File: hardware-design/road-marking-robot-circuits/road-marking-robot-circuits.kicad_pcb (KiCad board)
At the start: 2 copper layers, 56 parts, among them J1 12V_BATT, J10 MOTOR_1, J11 MOTOR_2, J13 PNEUMATIC_PUMP, J2 u-sonic-1, J3 u-sonic-2, J4 u-sonic-3, J5 u-sonic-4, J6 u-sonic-5, J7 FLOW_METER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

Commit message: [UPDATES] arduino position
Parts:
- removed Q1: PMOS, Package_TO_SOT_THT:TO-220-3_Vertical
- removed R1: R, Resistor_THT:R_Axial_DIN0309_L9.0mm_D3.2mm_P20.32mm_Horizontal
- added ACC1: GY-521, MPU6050-MODULE:GY-521, F.Cu at (510.4, 77.1)
- D1: value D_Zener -> 1N4001; footprint Diode_THT:D_DO-15_P12.70mm_Horizontal -> Diode_THT:D_DO-41_SOD81_P10.16mm_Horizontal
- J7: footprint Connector_PinHeader_2.54mm:PinHeader_1x02_P2.54mm_Vertical -> Connector_PinHeader_2.54mm:PinHeader_1x03_P2.54mm_Vertical
- R2, R3, R4: footprint Resistor_THT:R_Axial_DIN0309_L9.0mm_D3.2mm_P20.32mm_Horizontal -> Resistor_THT:R_Axial_DIN0309_L9.0mm_D3.2mm_P12.70mm_Horizontal
- moved BZ1 552.1 mm to (656.3, 85.0)
- moved D3 552.1 mm to (681.5, 62.3)
- moved D4 552.1 mm to (681.5, 66.6)
- moved D5 552.1 mm to (627.6, 80.0)
- moved J7 552.1 mm to (695.9, 81.5)
- moved J8 552.1 mm to (700.5, 81.5)
- moved J9 552.1 mm to (705.2, 81.5)
- moved Q2 552.1 mm to (627.9, 57.5)
- moved Q3 552.1 mm to (627.9, 63.3)
- moved Q4 552.1 mm to (627.9, 69.1)
- moved R3 552.1 mm to (695.1, 72.1)
- moved U5 552.1 mm to (668.8, 34.7)
- moved A1 525.1 mm to (572.0, -32.9), turned to 180 degrees
- moved D2 476.4 mm to (554.1, 110.8)
- moved D1 462.9 mm to (546.5, 106.0)
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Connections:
- D2 pad 2: Net-(D2-A) -> Net-(D1-A)
- SW1 pad 2: Net-(D2-A) -> Net-(D1-A)

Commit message: [UPDATES] PCB design
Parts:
- added D11: ACTIVE?, LED_THT:LED_D3.0mm, F.Cu at (489.3, 113.6)
- added D12: ACTIVE?, LED_THT:LED_D3.0mm, F.Cu at (491.2, 87.6)
- added D13: ACTIVE?, LED_THT:LED_D3.0mm, F.Cu at (490.6, 61.5)
- added H1: MountingHole, MountingHole:MountingHole_3.2mm_M3, F.Cu at (466.4, -46.0)
- added H2: MountingHole, MountingHole:MountingHole_3.2mm_M3, F.Cu at (573.3, -45.9)
- added H3: MountingHole, MountingHole:MountingHole_3.2mm_M3, F.Cu at (573.3, 136.8)
- added H4: MountingHole, MountingHole:MountingHole_3.2mm_M3, F.Cu at (466.0, 136.8)
- added R1: R, Resistor_THT:R_Axial_DIN0309_L9.0mm_D3.2mm_P12.70mm_Horizontal, F.Cu at (488.9, 116.2)
- added R5: R, Resistor_THT:R_Axial_DIN0309_L9.0mm_D3.2mm_P12.70mm_Horizontal, F.Cu at (490.9, 89.9)
- added R6: R, Resistor_THT:R_Axial_DIN0309_L9.0mm_D3.2mm_P12.70mm_Horizontal, F.Cu at (490.2, 64.0)
- J13, J8, J9: footprint Connector_PinHeader_2.54mm:PinHeader_1x02_P2.54mm_Vertical -> TerminalBlock:TerminalBlock_bornier-2_P5.08mm
- J7: footprint Connector_PinHeader_2.54mm:PinHeader_1x03_P2.54mm_Vertical -> TerminalBlock:TerminalBlock_bornier-3_P5.08mm
- Q2, Q3, Q4: footprint Package_TO_SOT_THT:TO-92_Inline -> Package_TO_SOT_THT:TO-92_Inline_Wide
- moved J9 238.3 mm to (467.4, 66.5), turned to -90 degrees
- moved J8 233.6 mm to (467.1, 91.2), turned to -90 degrees
- moved J7 216.6 mm to (486.1, 135.4), turned to 180 degrees
- moved D3 189.1 mm to (494.8, 92.2), turned to -90 degrees
- moved D4 187.5 mm to (494.0, 66.2), turned to -90 degrees
- moved R3 180.8 mm to (515.2, 91.0)
- moved U5 167.2 mm to (509.3, 84.8), turned to 90 degrees
- moved Q4 155.3 mm to (477.5, 107.9)
- moved Q2 152.1 mm to (477.7, 81.8)
- moved Q3 148.9 mm to (479.2, 55.8)
- moved BZ1 142.0 mm to (515.5, 103.5)
- moved J13 133.7 mm to (466.7, 118.0), turned to -90 degrees
- moved D5 115.3 mm to (512.8, 91.1), turned to 180 degrees
- moved K3 106.2 mm to (472.9, 113.9), turned to 0 degrees
- moved D10 103.1 mm to (492.8, 118.5)
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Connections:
- A1 pad D14: unconnected-(A1-D14/TX3-PadD14) -> /IN1
- A1 pad D15: unconnected-(A1-D15/RX3-PadD15) -> /IN2
- A1 pad D16: unconnected-(A1-D16/TX2-PadD16) -> /IN3
- A1 pad D17: unconnected-(A1-D17/RX2-PadD17) -> /IN4
- A1 pad D23: unconnected-(A1-PadD23) -> /US1_TR
- A1 pad D25: unconnected-(A1-PadD25) -> /US1_EC
- A1 pad D26: /IN4 -> unconnected-(A1-PadD26)
- A1 pad D27: /IN3 -> /US2_TR
- A1 pad D28: /IN2 -> unconnected-(A1-PadD28)
- A1 pad D29: /IN1 -> /US2_EC
- A1 pad D30: /US1_TR -> unconnected-(A1-PadD30)
- A1 pad D31: /US2_TR -> /US3_TR
- A1 pad D32: /US3_TR -> unconnected-(A1-PadD32)
- A1 pad D33: /US4_TR -> /US3_EC
- A1 pad D34: /US5_TR -> unconnected-(A1-PadD34)
- A1 pad D35: /US1_EC -> /US4_TR
- A1 pad D36: /US2_EC -> unconnected-(A1-PadD36)
- A1 pad D37: /US3_EC -> /US4_EC
- A1 pad D38: /US4_EC -> unconnected-(A1-PadD38)
- A1 pad D39: /US5_EC -> /US5_TR
- A1 pad D41: Net-(BZ1-+) -> /US5_EC
- BZ1 pad 1: Net-(BZ1-+) -> unconnected-(BZ1-+-Pad1)
- BZ1 pad 2: Earth -> unconnected-(BZ1---Pad2)
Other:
- board outline added: 114.2 x 189.8 mm

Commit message: updates FIRMWARE for ARDUINO
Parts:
- removed D6, D7, D8, D9: 1N4001, Diode_THT:D_DO-41_SOD81_P10.16mm_Horizontal
- removed J10: MOTOR_1, TerminalBlock:TerminalBlock_bornier-2_P5.08mm
- removed J11: MOTOR_2, TerminalBlock:TerminalBlock_bornier-2_P5.08mm
- removed J7: FLOW_METER, TerminalBlock:TerminalBlock_bornier-3_P5.08mm
- removed U6: L293D, Package_DIP:DIP-16_W7.62mm
- added D14: 1N4001, Diode_THT:D_DO-41_SOD81_P10.16mm_Horizontal, F.Cu at (514.4, 124.8)
- added D15: 3mm Red LED, LED_THT:LED_D3.0mm, F.Cu at (519.6, 99.5)
- added J12: 2PIN terminal block, TerminalBlock:TerminalBlock_bornier-2_P5.08mm, F.Cu at (523.0, 134.8)
- added J14: MOTOR_DRIVER, TerminalBlock:TerminalBlock_Xinya_XY308-2.54-8P_1x08_P2.54mm_Horizontal, F.Cu at (570.5, 25.6)
- added K4: SugarCube relay, Relay_THT:Relay_SPDT_Finder_36.11, F.Cu at (531.4, 126.2)
- added Q1: BC547 transistor, Package_TO_SOT_THT:TO-92_Inline_Wide, F.Cu at (528.3, 106.7)
- added R7: 500R resistor, Resistor_THT:R_Axial_DIN0309_L9.0mm_D3.2mm_P12.70mm_Horizontal, F.Cu at (522.0, 99.6)
- ACC1: value GY-521 -> mpu6050
- C1, C2, C3, C4, C5, C6, C7, C8: value C -> 10uf Capcaitor
- D11, D12, D13: value ACTIVE? -> 3mm Red LED
- D2, D5: value LED -> 3mm Green LED
- HS1: value 12V -> Heat sink
- HS2: value 6V -> Heat sink
- HS3: value 9V -> Heat sink
- HS4: value 5V -> Heat sink
- J1: value 12V_BATT -> DC Barrel Jack THT
- J13: value PNEUMATIC_PUMP -> 2PIN terminal block
- J8: value 12V_SOLENOID -> 2PIN terminal block
- J9: value SPRAY_GUN -> 2 pin Terminal block
- K1, K2, K3: value FINDER-36.11 -> SugarCube relay
- Q2, Q3, Q4: value BC547 -> BC547 transistor
- R1, R2, R3, R5, R6: value R -> 500R resistor
- R4: value 10K -> 10K resistor
- SW1: value SW_SPST -> 2pin terminal block
- SW2: value RESET -> push button pin
- U5: value ~ -> NE06M GPS Module
- moved BZ1 82.1 mm to (476.8, 31.2), turned to 180 degrees
- moved R3 53.8 mm to (481.1, 49.4), turned to 180 degrees
- moved D5 50.9 mm to (483.5, 49.5), turned to 0 degrees
- moved ACC1 27.1 mm to (509.8, 30.5), turned to -90 degrees
- moved C7 13.1 mm to (556.5, 70.4)
- moved C1 13.1 mm to (555.7, 50.0)
- moved C2 13.1 mm to (555.7, 57.1)
- moved C8 13.1 mm to (556.5, 65.6)
- moved HS1 13.1 mm to (564.5, 52.8)
- moved HS3 13.1 mm to (564.6, 66.8)
- moved U2 13.1 mm to (560.6, 50.9)
- moved C3 13.1 mm to (556.2, 78.5)
- moved C4 13.1 mm to (556.0, 85.2)
- moved C5 13.1 mm to (557.3, 91.3)
- moved C6 13.1 mm to (556.5, 97.0)
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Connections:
- A1 pad A10: unconnected-(A1-PadA10) -> /PUMP2_ACTIVATE
- A1 pad A11: unconnected-(A1-PadA11) -> /BUZZER
- A1 pad A12: unconnected-(A1-PadA12) -> /USER_LED
- A1 pad D37: /US4_EC -> unconnected-(A1-PadD37)
- A1 pad D39: /US5_TR -> unconnected-(A1-PadD39)
- A1 pad D40: /USER_LED -> unconnected-(A1-PadD40)
- A1 pad D41: /US5_EC -> unconnected-(A1-PadD41)
- A1 pad D43: unconnected-(A1-PadD43) -> /US4_EC
- A1 pad D45: unconnected-(A1-PadD45) -> /US5_TR
- A1 pad D47: unconnected-(A1-PadD47) -> /US5_EC
- BZ1 pad 1: unconnected-(BZ1-+-Pad1) -> /BUZZER
- BZ1 pad 2: unconnected-(BZ1---Pad2) -> Earth
- J6 pad 2: /US5_EC -> 5V_REG
- J6 pad 3: /US5_TR -> /US5_EC
- J6 pad 4: 5V_REG -> /US5_TR
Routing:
- net Earth: track 0.00 -> 761.5 mm, vias 0 -> 14
- net 5V_REG: track 0.00 -> 685.1 mm, vias 0 -> 11
- net /PUMP2_ACTIVATE: track 0.00 -> 172.9 mm, vias 0 -> 2
- net /FLOW_METER: track 0.00 -> 167.3 mm, vias 0 -> 2
- net /PUMP_ACTIVATE: track 0.00 -> 166.8 mm
- net 12V_REG: track 0.00 -> 163.9 mm, vias 0 -> 2
- net 12V_UNREG: track 0.00 -> 139.0 mm, vias 0 -> 4
- net /SOLND_REL: track 0.00 -> 121.5 mm, vias 0 -> 2
- net /IN4: track 0.00 -> 103.9 mm
- net /IN3: track 0.00 -> 103.3 mm
- net /SPRAY_GUN_REL: track 0.00 -> 102.6 mm, vias 0 -> 2
- net /IN2: track 0.00 -> 100.8 mm
- net /IN1: track 0.00 -> 98.7 mm
- net Net-(D10-A): track 0.00 -> 78.0 mm
- net /GPS_TX: track 0.00 -> 73.4 mm
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
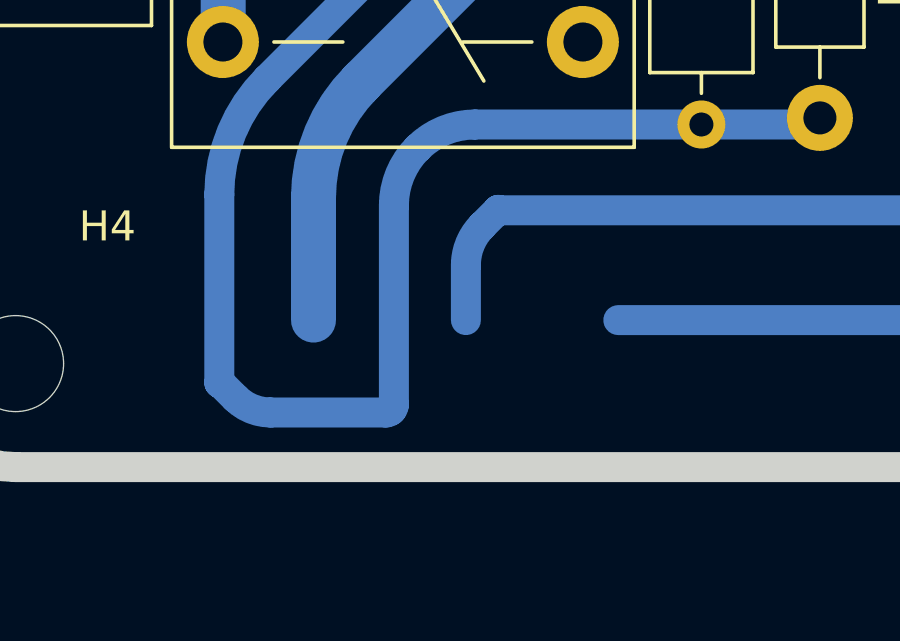
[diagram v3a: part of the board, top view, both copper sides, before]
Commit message: adds motor control code
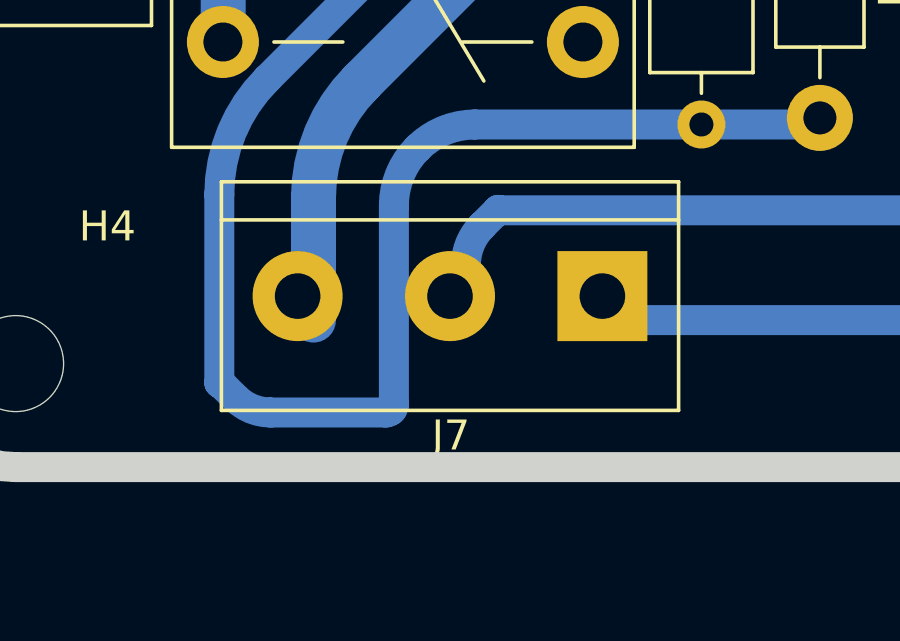
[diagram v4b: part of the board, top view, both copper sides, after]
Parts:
- added J7: 3PIN Terminal block, TerminalBlock:TerminalBlock_bornier-3_P5.08mm, F.Cu at (485.6, 134.6)
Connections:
- J8 pad 1: Net-(J8-Pin_1) -> 12V_UNREG
- K1 pad 11: Net-(J8-Pin_1) -> Earth
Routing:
- net Net-(J8-Pin_1): track 18.6 -> 0.00 mm
- net (no net): track 0.00 -> 18.6 mm
